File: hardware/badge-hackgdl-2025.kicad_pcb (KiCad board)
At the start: 11 copper layers, 73.4 x 79.5 mm, 54 parts, among them J1 ADDON, J2 Battery, P1 USB_C_Plug_USB2.0, Q1 DMG3415U-7, Q2 MMBT2222A, SW1 ON, SW2 RESET, SW3 BOOT, SW4 RIGHT, SW5 BACK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

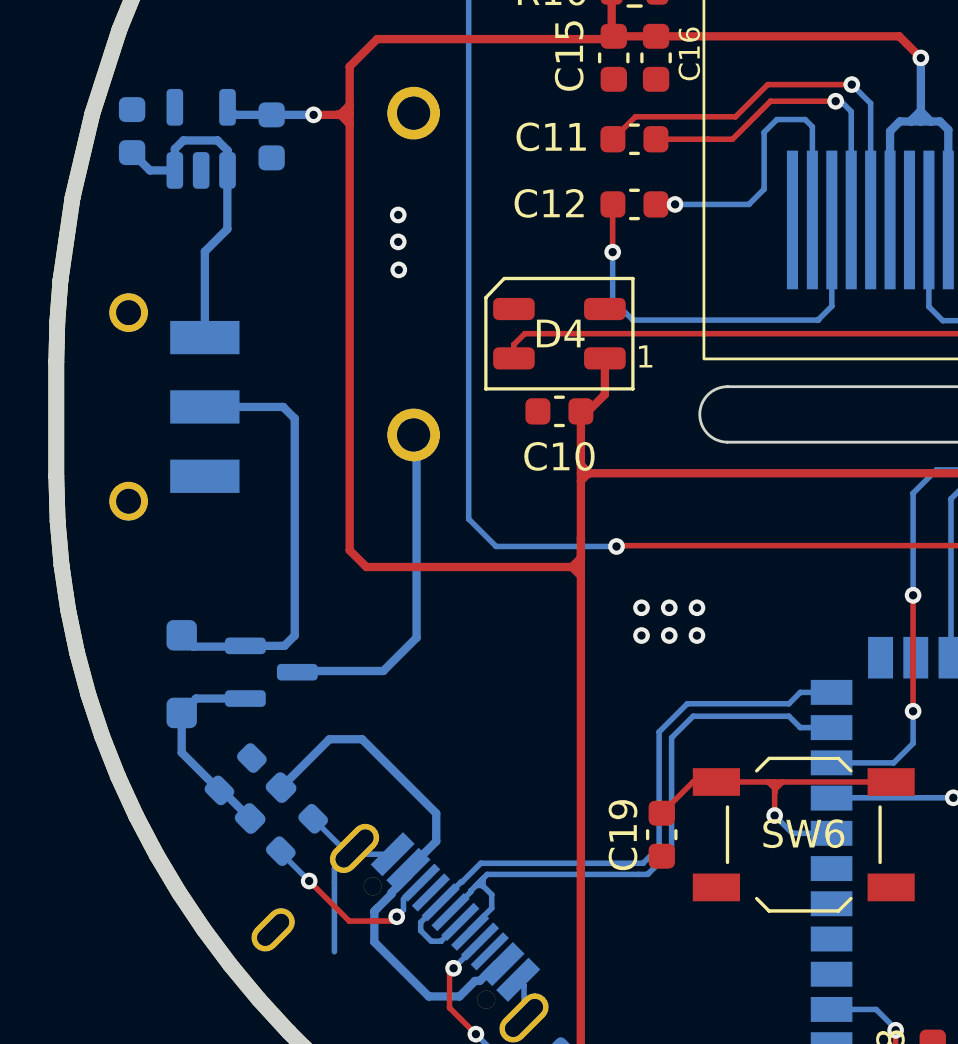
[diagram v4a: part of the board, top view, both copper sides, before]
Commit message: feat(hw): change LDO position
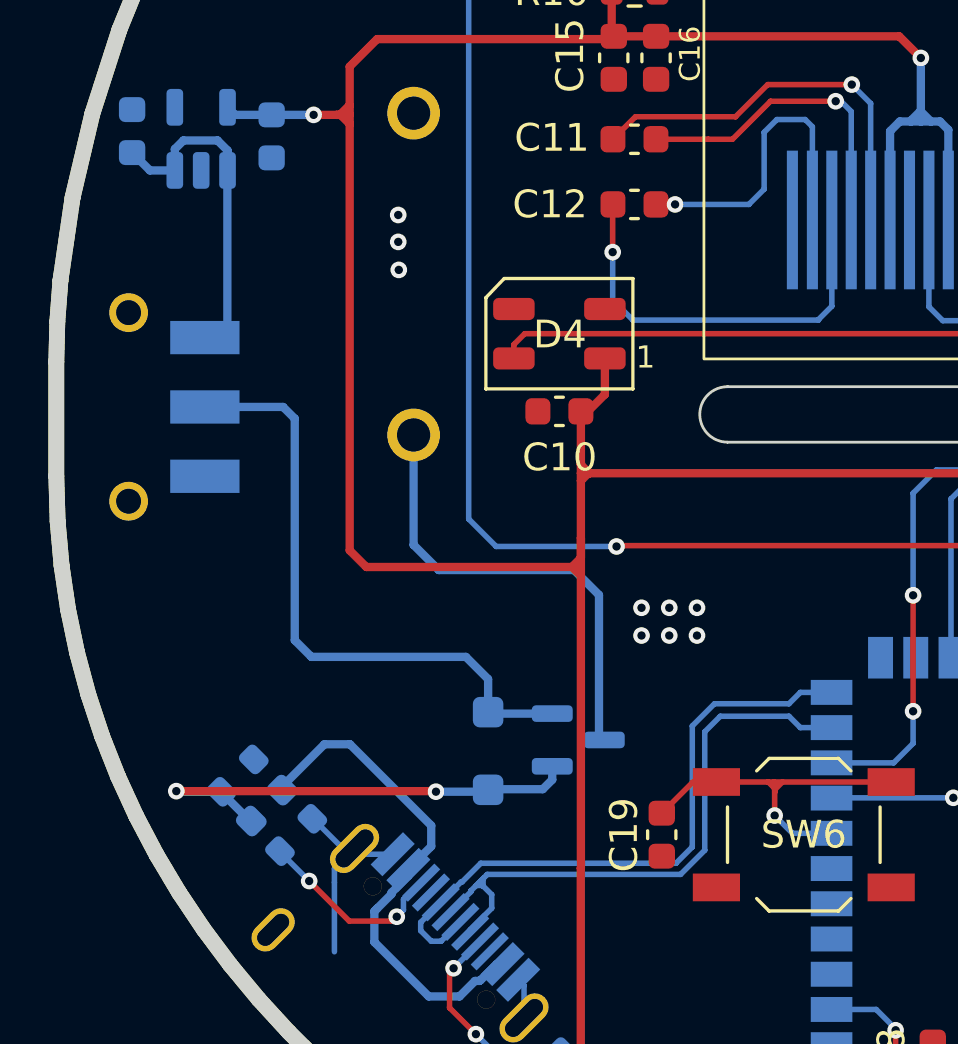
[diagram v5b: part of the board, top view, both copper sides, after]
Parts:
- moved D1 11.4 mm to (112.5, 76.8)
- moved Q1 11.3 mm to (115.8, 76.4)
- moved F1 0.10 mm to (104.6, 78.7)
- moved R3 0.09 mm to (103.5, 77.7)
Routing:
- net VBUS: track 7.39 -> 17.8 mm, vias 0 -> 2
- net Net-(D1-K): track 15.6 -> 22.5 mm
- net +BATT: track 12.2 -> 16.7 mm
- net Net-(F1-Pad1): track 18.9 -> 18.3 mm

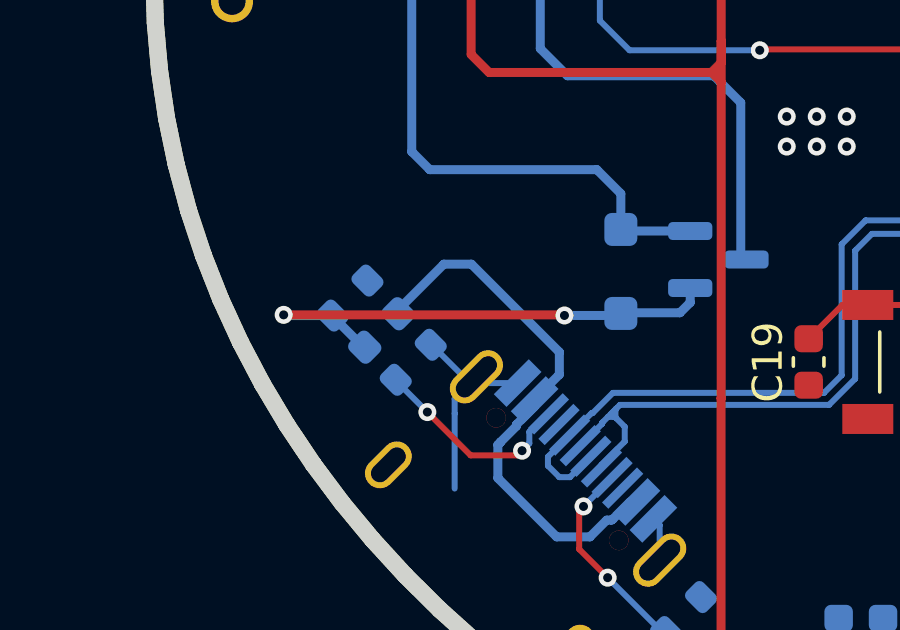
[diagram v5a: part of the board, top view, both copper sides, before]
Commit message: feat(hw): change F1 position
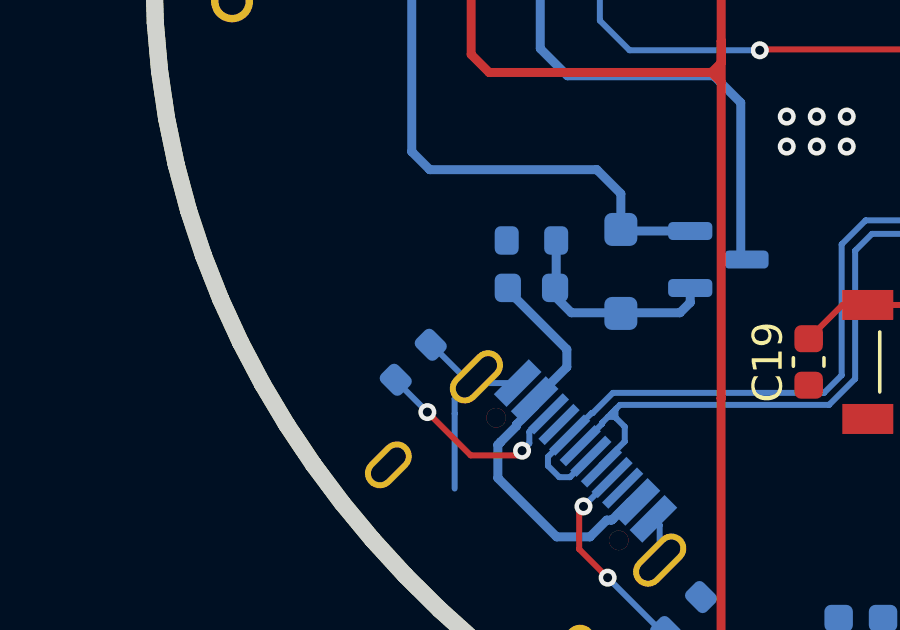
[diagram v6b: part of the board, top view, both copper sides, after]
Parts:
- moved R3 6.35 mm to (109.6, 75.7), turned to 180 degrees
- moved F1 5.20 mm to (109.6, 77.3), turned to 0 degrees
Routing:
- net VBUS: track 17.8 -> 7.68 mm, vias 2 -> 0
- net Net-(F1-Pad1): track 18.3 -> 14.0 mm

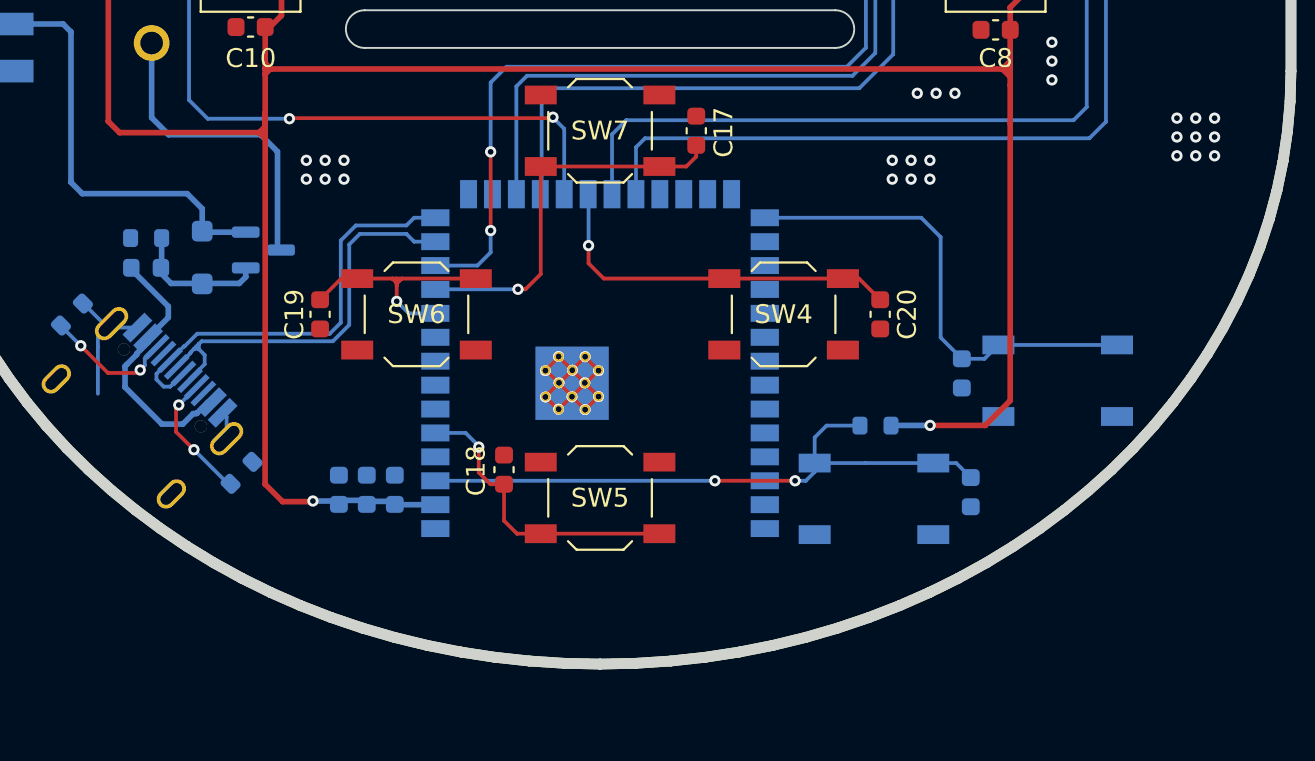
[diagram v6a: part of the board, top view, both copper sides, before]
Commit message: feat(hw): add labels
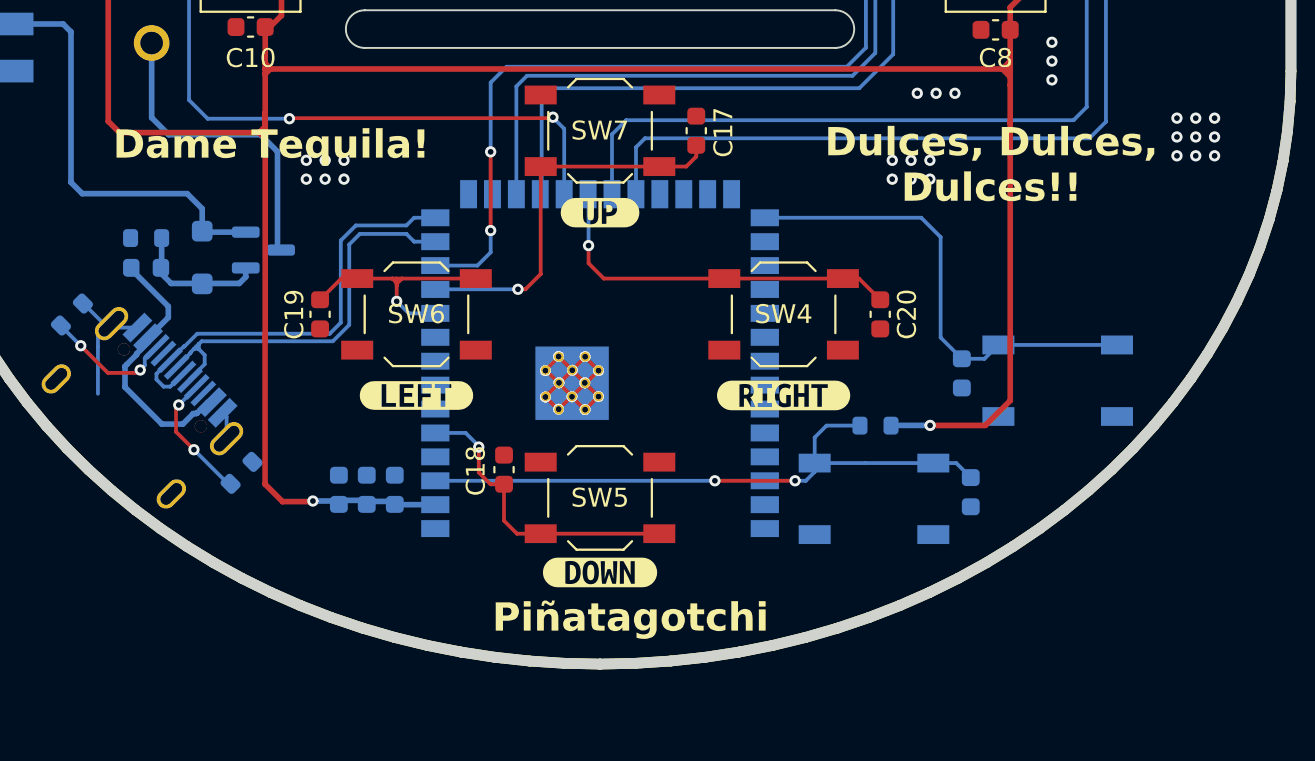
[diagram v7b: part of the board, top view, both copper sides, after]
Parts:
- added G***: LOGO, Aesthetics:electronic_cats_logo_8x6, B.Cu at (165.1, 62.4)
- added kibuzzard-678830B0: G***, kibuzzard-678830B0, B.Cu at (102.7, 70.3)
- added kibuzzard-678830B8: G***, kibuzzard-678830B8, B.Cu at (102.7, 58.6)
- added kibuzzard-678830C2: G***, kibuzzard-678830C2, F.Cu at (133.7, 74.4)
- added kibuzzard-678830E5: G***, kibuzzard-678830E5, F.Cu at (133.7, 93.5)
- added kibuzzard-678830ED: G***, kibuzzard-678830ED, F.Cu at (123.9, 84.1)
- added kibuzzard-678830F7: G***, kibuzzard-678830F7, F.Cu at (143.4, 84.1)
- added kibuzzard-67883A3F: G***, kibuzzard-67883A3F, B.Cu at (148.2, 93.4)
- added kibuzzard-67883A4C: G***, kibuzzard-67883A4C, B.Cu at (158.1, 79.3)
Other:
- board text added: "Badge HackGDL 2025 v2.0"
- board text added: "Dame Tequila!"
- board text added: "Dulces, Dulces, Dulces!!"
- board text added: "Piñatagotchi"

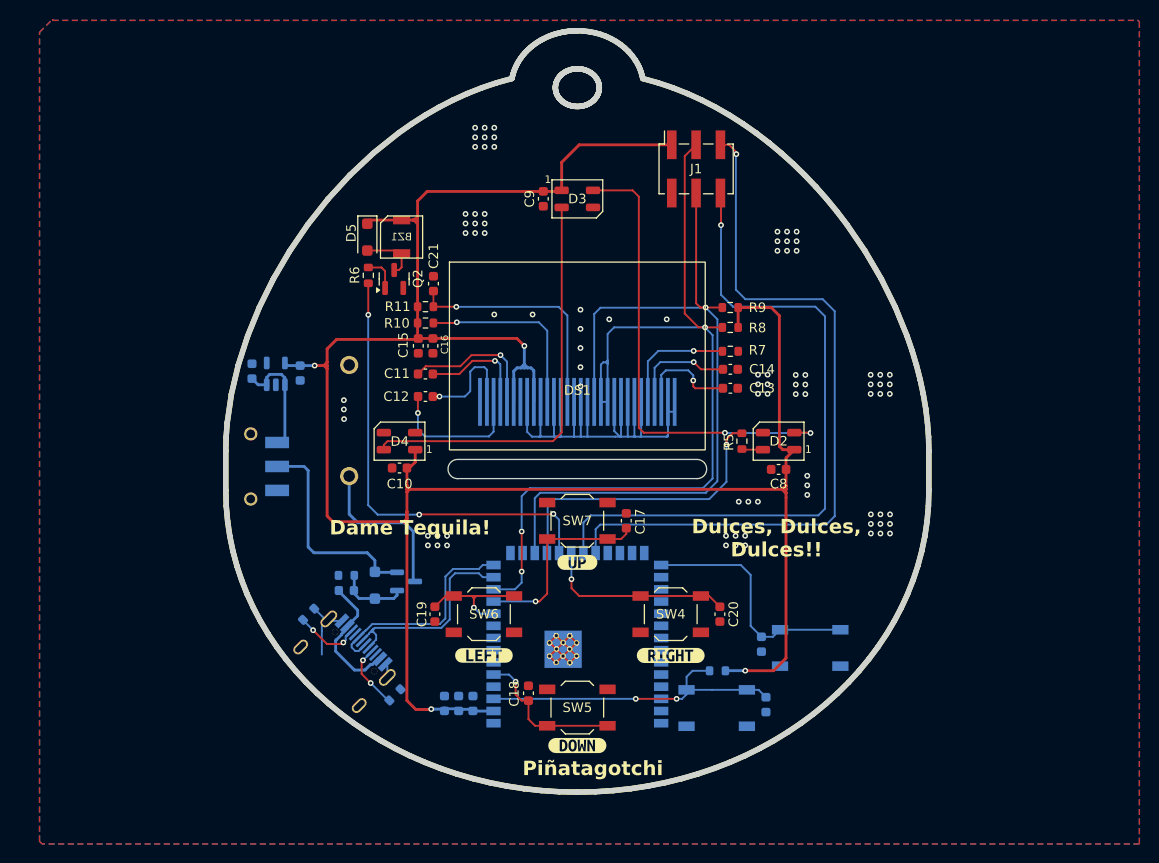
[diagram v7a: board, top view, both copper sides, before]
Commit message: refactor(hw): move buttons
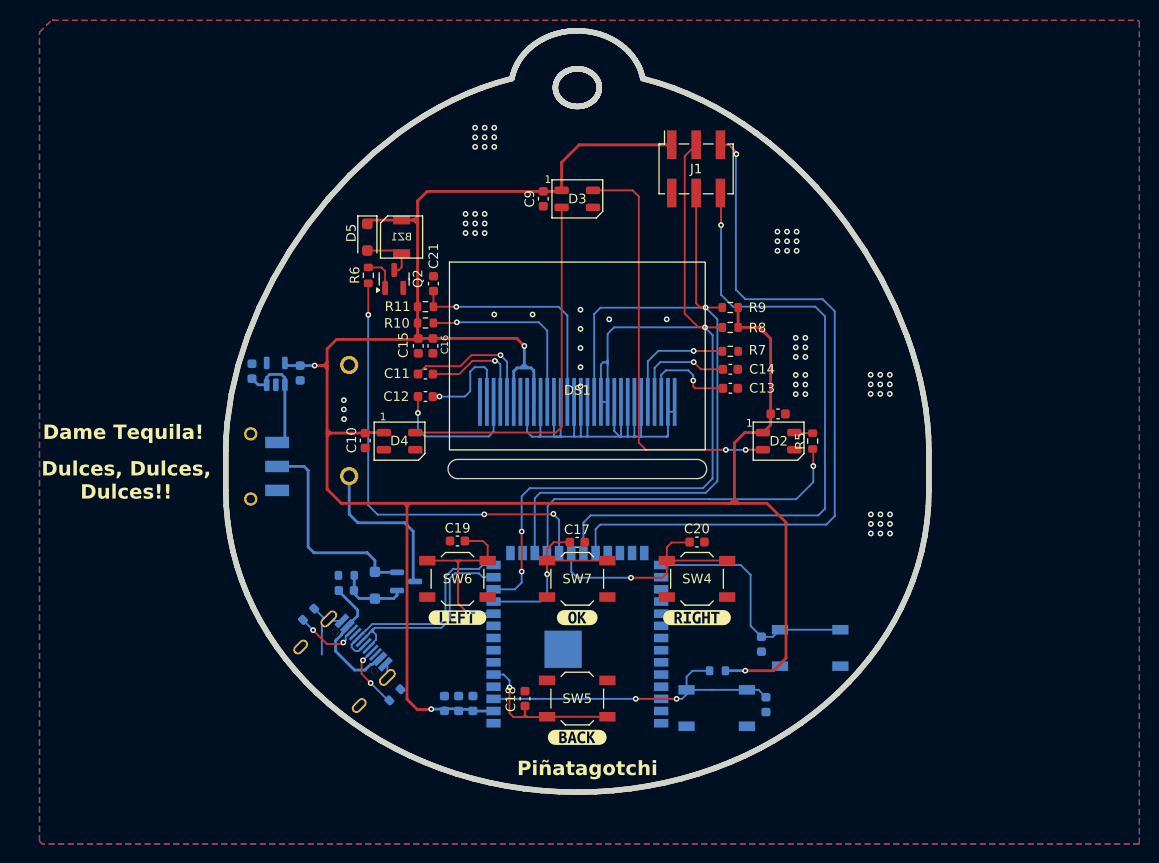
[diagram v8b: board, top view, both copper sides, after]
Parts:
- removed kibuzzard-678830C2: G***, kibuzzard-678830C2
- removed kibuzzard-678830E5: G***, kibuzzard-678830E5
- added kibuzzard-67898922: G***, kibuzzard-67898922, F.Cu at (133.7, 80.1)
- added kibuzzard-6789895F: G***, kibuzzard-6789895F, F.Cu at (133.7, 92.6)
- moved C19 8.00 mm to (121.2, 72.1), turned to 180 degrees
- moved C20 7.90 mm to (146.2, 72.2), turned to 0 degrees
- moved R5 7.38 mm to (158.2, 61.7), turned to 90 degrees
- moved SW7 6.06 mm to (133.7, 76.1), turned to 180 degrees
- moved C8 5.79 mm to (154.6, 58.9), turned to 180 degrees
- moved C17 5.59 mm to (133.7, 72.3), turned to 0 degrees
- moved kibuzzard-678830ED 4.82 mm to (121.2, 80.1)
- moved kibuzzard-678830F7 4.81 mm to (146.2, 80.1)
- moved SW6 4.61 mm to (121.2, 76.1)
- moved SW4 4.60 mm to (146.2, 76.1)
- moved C10 4.59 mm to (111.5, 61.7), turned to 90 degrees
- moved SW5 0.94 mm to (133.7, 88.6)
- moved C18 0.67 mm to (128.2, 88.6)
- turned D2 to 0 degrees
- turned D4 to 0 degrees
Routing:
- net GND: track 99.0 -> 83.0 mm, vias 99 -> 69
- net /LEFT: track 13.3 -> 19.7 mm
- net +3V3: track 247.8 -> 241.4 mm
- net /NEOPIXEL: track 31.0 -> 37.2 mm
- net Net-(D2-DOUT): track 49.0 -> 44.0 mm
- net Net-(D3-DOUT): track 43.1 -> 38.5 mm
- net /RIGHT: track 20.0 -> 24.0 mm
- net /BACK: track 16.1 -> 17.6 mm
- net /MIDDLE: track 20.7 -> 19.6 mm
